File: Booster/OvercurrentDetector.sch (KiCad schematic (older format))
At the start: 9 parts

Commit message: Somewhat optimistic circuit to add delay to overcurrent sensing and release.
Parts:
- removed U?: LM339, symbol LM339
- added C? (x2): C, symbol C
- added D?: D, symbol D
- added R?: 5.6K, symbol R
- added R?: 2.7K, symbol R
- added R? (x2): R, symbol R
- added RV? (x2): POT_TRIM, symbol POT_TRIM
- added U?: LM339, symbol LM339
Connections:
- net labels added: ~Overcurrent
- net labels removed: Overcurrent
- wire segments 20 -> 44
- no-connect marks 0 -> 3
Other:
- note added: "Detect."
- note added: "Sense & release delay"
- note added: "Sensitivity"
- moved on the sheet: R?, RV?

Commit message: Trim pots to comparitors now set up to use fewer resistors. Added status sheet, currently not doing anything useful.
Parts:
- removed D?: D, symbol D
- removed R?: 5.6K, symbol R
- removed R?: 2.7K, symbol R
- removed R?: R, symbol R
- removed RV?: POT_TRIM, symbol POT_TRIM
- added C?: 220µF, symbol C
- added R?: 10K, symbol R
- added R?: 2K, symbol R
- added R?: 100R, symbol R
- added RV?: 10K, symbol POT_TRIM
- added U?: LM339, symbol LM339
- RV?: value POT_TRIM -> 10K
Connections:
- wire segments 44 -> 43
- no-connect marks 3 -> 1
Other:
- note added: "Release delay\n0.5s - ~~10s"
- note added: "Sense delay"
- note removed: "Sense & release delay"
- moved on the sheet: C?, RV?, U?C

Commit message: Working on replacing over current detection to overcurrent protection.
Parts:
- added C? (x3): C, symbol C
- added R? (x10): 10K, symbol R
- added R?: 1K, symbol R
- added R? (x2): 0.1, symbol R
- added RV?: 50K, symbol POT_TRIM
- added RV? (x3): 10K, symbol POT_TRIM
- added U?: LM338, TO_SOT_Packages_THT:TO-220_Vertical, symbol LM350_TO220
- added U? (x2): LM358, symbol LM358
- added U? (x3): LM339, symbol LM339
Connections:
- net labels added: SENSE_drop, SENSE_high, SENSE_low, VCC_Driver
- wire segments 43 -> 134
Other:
- note added: "Detect delay"
- note added: "Filter 2 µs\nshort clear"
- note added: "Release delay"
- note added: "SENSE_high - SENSE_low"
- note added: "SENSE_high - X * SENSE_drop"
- moved on the sheet: C?, R?, RV?, U?A, U?B, U?C, U?D

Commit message: Over current protection and detection - with detection delay and release delay.
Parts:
- removed C? (x5): C, symbol C
- removed C?: 220µF, symbol C
- removed R? (x4): R, symbol R
- removed R? (x11): 10K, symbol R
- removed R?: 2K, symbol R
- removed R?: 100R, symbol R
- removed R?: 1K, symbol R
- removed RV?: 200K, symbol POT_TRIM
- removed RV? (x5): 10K, symbol POT_TRIM
- removed RV?: 50K, symbol POT_TRIM
- removed U? (x7): LM339, symbol LM339
- removed U? (x2): LM358, symbol LM358
- added C? (x2): .1µF, symbol C
- added C? (x2): 100µF, symbol C
- added R? (x6): 10K, symbol R
- added R?: 22K, symbol R
- added R?: R, symbol R
- added RV? (x2): 1K, symbol POT_TRIM
- added RV? (x2): 10K, symbol POT_TRIM
- added U? (x2): LM358, symbol LM358
- added U? (x3): LM339, symbol LM339
- R?: value 1K -> 2.8K
- R?: value 39K -> 10K
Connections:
- net labels added: +15V
- net labels removed: +12V, Driver1A, Driver1B, SENSE_drop, SENSE_high, SENSE_low, Track1A, Track1B
- wire segments 134 -> 65
- no-connect marks 1 -> 0
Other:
- note added: "Current Limiter"
- note added: "Release delay\nlow = short"
- note added: "Rsense"
- note added: "Sense delay\nhigh = short"
- note removed: "Detect delay"
- note removed: "Detect."
- note removed: "Filter 2 µs\nshort clear"
- note removed: "Release delay"
- note removed: "Release delay\n0.5s - ~~10s"
- note removed: "SENSE_high - SENSE_low"
- note removed: "SENSE_high - X * SENSE_drop"
- note removed: "Sense delay"
- moved on the sheet: R?, U?

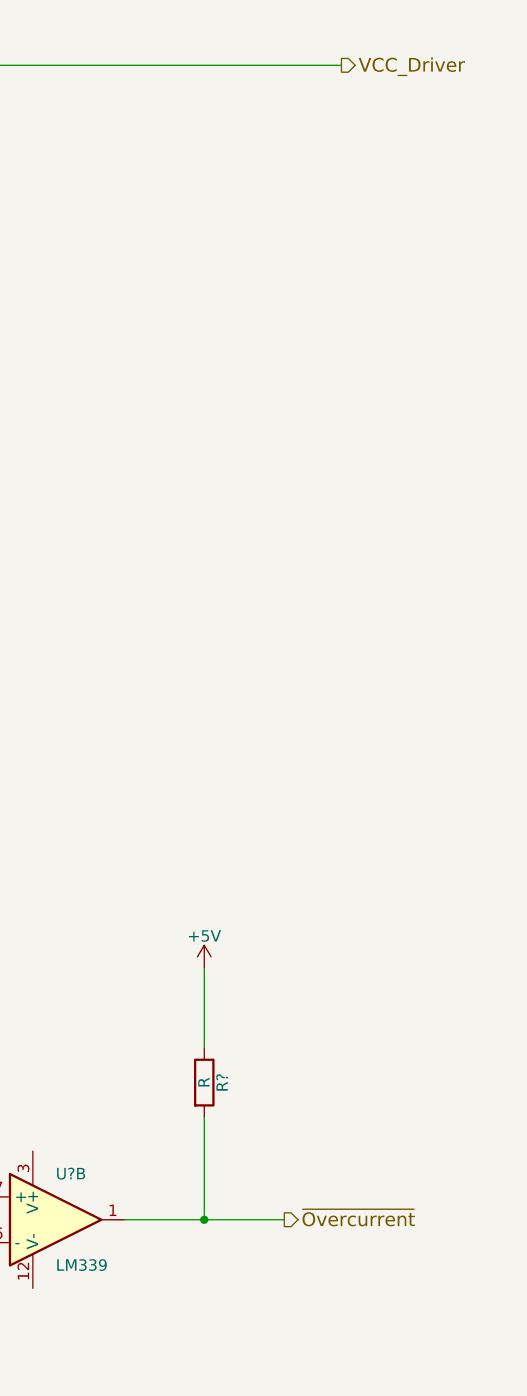
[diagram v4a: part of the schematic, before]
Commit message: Added reversing support. Working on status output.
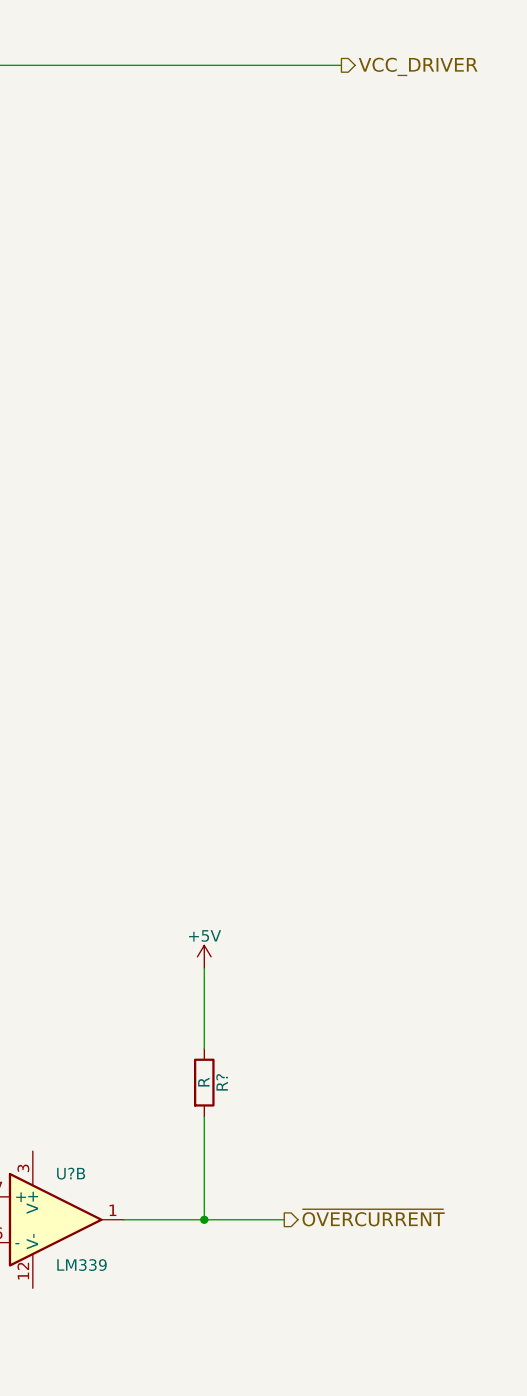
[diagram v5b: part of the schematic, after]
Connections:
- net VCC_Driver renamed VCC_DRIVER
- net ~Overcurrent renamed ~OVERCURRENT
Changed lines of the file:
@@
 $Descr A4 11693 8268
 encoding utf-8
-Sheet 5 6
+Sheet 5 7
 Title ""
 Date ""
@@
 $EndDescr
 Text HLabel 8100 6050 2    60   Output ~ 0
-~Overcurrent
+~OVERCURRENT
 $Comp
 L R R?
@@
 $EndComp
 Text HLabel 8350 1000 2    60   Output ~ 0
-VCC_Driver
+VCC_DRIVER
 $Comp
 L LM358 U?

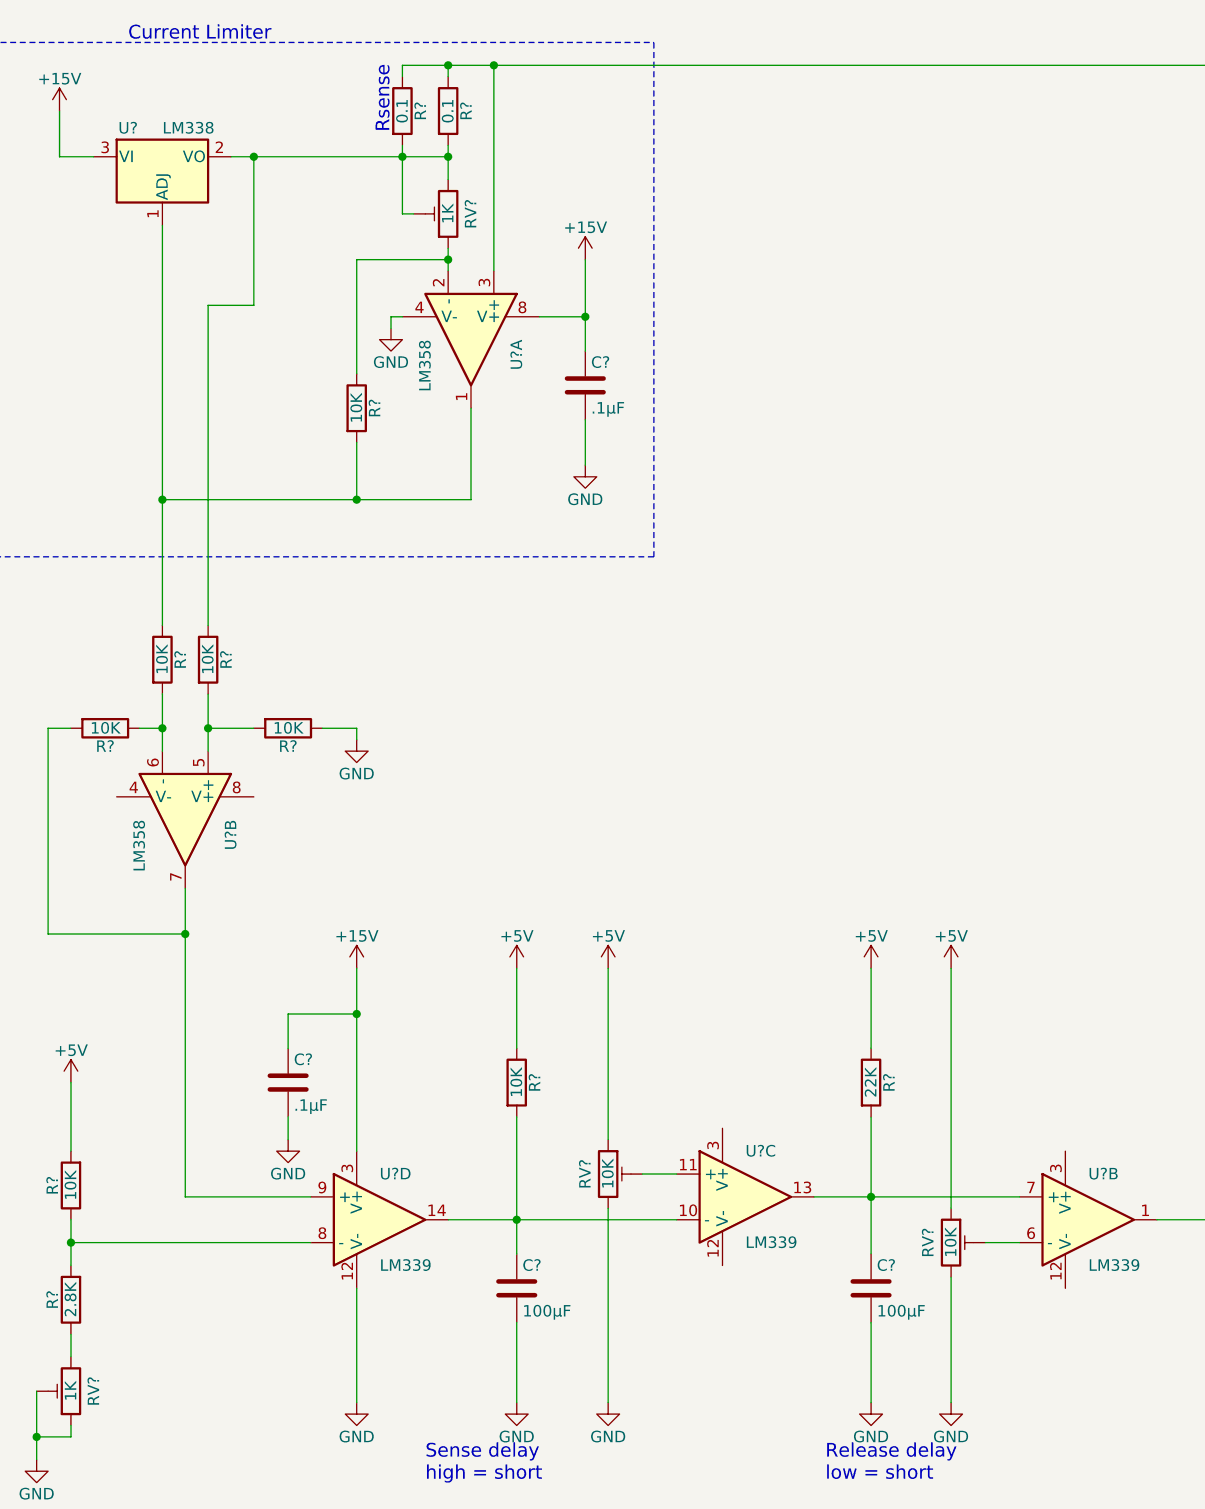
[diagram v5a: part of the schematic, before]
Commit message: Added meassurement tabs and other general "finalizing touches"
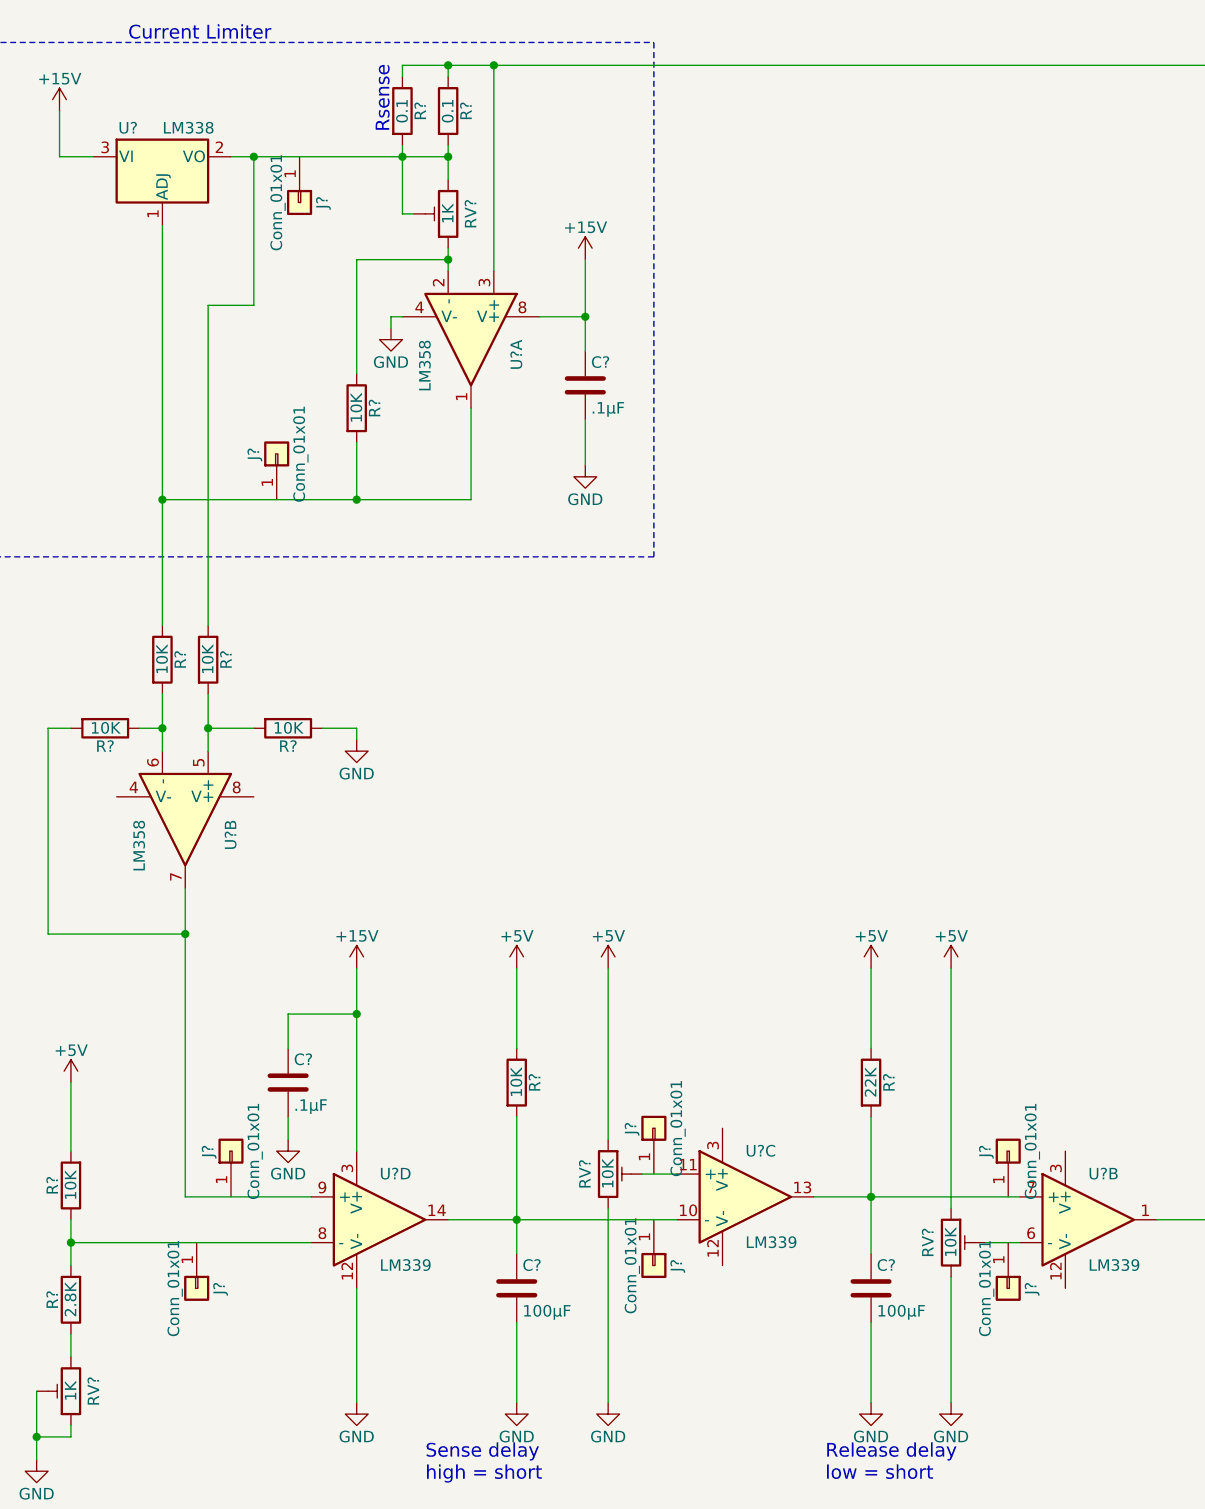
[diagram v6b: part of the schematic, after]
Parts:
- added J? (x8): Conn_01x01, symbol Conn_01x01
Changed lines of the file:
@@
 	1    0    0    -1
 $EndComp
+$Comp
+L Conn_01x01 J?
+U 1 1 5A0F905B
+P 3200 6350
+F 0 "J?" H 3200 6450 50  0000 C CNN
+F 1 "Conn_01x01" H 3200 6250 50  0000 C CNN
+F 2 "" H 3200 6350 50  0001 C CNN
+F 3 "" H 3200 6350 50  0001 C CNN
+	1    3200 6350
+	0    1    1    0
+$EndComp
+$Comp
+L Conn_01x01 J?
+U 1 1 5A0F90DB
+P 5200 6250
+F 0 "J?" H 5200 6350 50  0000 C CNN
+F 1 "Conn_01x01" H 5200 6150 50  0000 C CNN
+F 2 "" H 5200 6250 50  0001 C CNN
+F 3 "" H 5200 6250 50  0001 C CNN
+	1    5200 6250
+	0    1    1    0
+$EndComp
+$Comp
+L Conn_01x01 J?
+U 1 1 5A0F915B
+P 5200 5650
+F 0 "J?" H 5200 5750 50  0000 C CNN
+F 1 "Conn_01x01" H 5200 5550 50  0000 C CNN
+F 2 "" H 5200 5650 50  0001 C CNN
+F 3 "" H 5200 5650 50  0001 C CNN
+	1    5200 5650
+	0    -1   -1   0
+$EndComp
+$Comp
+L Conn_01x01 J?
+U 1 1 5A0F966E
+P 6750 6350
+F 0 "J?" H 6750 6450 50  0000 C CNN
+F 1 "Conn_01x01" H 6750 6250 50  0000 C CNN
+F 2 "" H 6750 6350 50  0001 C CNN
+F 3 "" H 6750 6350 50  0001 C CNN
+	1    6750 6350
+	0    1    1    0
+$EndComp
+$Comp
+L Conn_01x01 J?
+U 1 1 5A0F96F2
+P 6750 5750
+F 0 "J?" H 6750 5850 50  0000 C CNN
+F 1 "Conn_01x01" H 6750 5650 50  0000 C CNN
+F 2 "" H 6750 5750 50  0001 C CNN
+F 3 "" H 6750 5750 50  0001 C CNN
+	1    6750 5750
+	0    -1   -1   0
+$EndComp
+$Comp
+L Conn_01x01 J?
+U 1 1 5A0F97B9
+P 3550 2700
+F 0 "J?" H 3550 2800 50  0000 C CNN
+F 1 "Conn_01x01" H 3550 2600 50  0000 C CNN
+F 2 "" H 3550 2700 50  0001 C CNN
+F 3 "" H 3550 2700 50  0001 C CNN
+	1    3550 2700
+	0    -1   -1   0
+$EndComp
+$Comp
+L Conn_01x01 J?
+U 1 1 5A0F985D
+P 3650 1600
+F 0 "J?" H 3650 1700 50  0000 C CNN
+F 1 "Conn_01x01" H 3650 1500 50  0000 C CNN
+F 2 "" H 3650 1600 50  0001 C CNN
+F 3 "" H 3650 1600 50  0001 C CNN
+	1    3650 1600
+	0    1    1    0
+$EndComp
+$Comp
+L Conn_01x01 J?
+U 1 1 5A0F9901
+P 3350 5750
+F 0 "J?" H 3350 5850 50  0000 C CNN
+F 1 "Conn_01x01" H 3350 5650 50  0000 C CNN
+F 2 "" H 3350 5750 50  0001 C CNN
+F 3 "" H 3350 5750 50  0001 C CNN
+	1    3350 5750
+	0    -1   -1   0
+$EndComp
 $EndSCHEMATC
